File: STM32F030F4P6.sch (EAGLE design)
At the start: 11 parts, among them J3 455-1750-1-ND, U1 STM32F030F4P6, U2 CJA1117B-3.3-SOT89

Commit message: Added capacitors, resistors, diodes, LEDs, and J-Link connector.
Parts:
- added C2, C3, C4, C5, C6, C7: (no value), adafruit:C-USC0603
- added D2: (no value), adafruit:DIODESOD-123
- added J4: CORTEX_DEBUG_MINIMUM_PTH, SparkFun-Connectors:CORTEX_DEBUG_MINIMUM_PTH
- added LED2: (no value), adafruit:LEDCHIPLED_0603
- added R2, R3, R4, R5: (no value), adafruit:R-US_R0603
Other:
- moved on the sheet: C1
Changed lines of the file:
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@@
 <part name="SUPPLY1" library="SparkFun-PowerSymbols" deviceset="VDD" device=""/>
 <part name="GND1" library="SparkFun-PowerSymbols" deviceset="GND" device=""/>
+<part name="R2" library="adafruit" deviceset="R-US_" device="R0603"/>
+<part name="R3" library="adafruit" deviceset="R-US_" device="R0603"/>
+<part name="R4" library="adafruit" deviceset="R-US_" device="R0603"/>
+<part name="R5" library="adafruit" deviceset="R-US_" device="R0603"/>
+<part name="C2" library="adafruit" deviceset="C-US" device="C0603"/>
+<part name="C3" library="adafruit" deviceset="C-US" device="C0603"/>
+<part name="C4" library="adafruit" deviceset="C-US" device="C0603"/>
+<part name="C5" library="adafruit" deviceset="C-US" device="C0603"/>
+<part name="C6" library="adafruit" deviceset="C-US" device="C0603"/>
+<part name="C7" library="adafruit" deviceset="C-US" device="C0603"/>
+<part name="LED2" library="adafruit" deviceset="LED" device="CHIPLED_0603"/>
+<part name="D2" library="adafruit" deviceset="DIODE" device="SOD-123"/>
+<part name="J4" library="SparkFun-Connectors" deviceset="CORTEX_DEBUG_MINIMUM" device="_PTH"/>
 </parts>
 <sheets>
@@
 </plain>
 <instances>
-<instance part="C1" gate="G$1" x="71.12" y="15.24" smashed="yes">
-<attribute name="NAME" x="72.136" y="15.875" size="1.778" layer="95"/>
-<attribute name="VALUE" x="72.136" y="11.049" size="1.778" layer="96"/>
+<instance part="C1" gate="G$1" x="20.32" y="17.78" smashed="yes">
+<attribute name="NAME" x="21.336" y="18.415" size="1.778" layer="95"/>
+<attribute name="VALUE" x="21.336" y="13.589" size="1.778" layer="96"/>
 </instance>
 <instance part="R1" gate="G$1" x="99.06" y="15.24" smashed="yes">
@@
 <attribute name="VALUE" x="215.9" y="111.506" size="1.778" layer="96" align="top-center"/>
 </instance>
+<instance part="R2" gate="G$1" x="99.06" y="10.16" smashed="yes">
+<attribute name="NAME" x="95.25" y="11.6586" size="1.778" layer="95"/>
+<attribute name="VALUE" x="95.25" y="6.858" size="1.778" layer="96"/>
+</instance>
+<instance part="R3" gate="G$1" x="99.06" y="5.08" smashed="yes">
+<attribute name="NAME" x="95.25" y="6.5786" size="1.778" layer="95"/>
+<attribute name="VALUE" x="95.25" y="1.778" size="1.778" layer="96"/>
+</instance>
+<instance part="R4" gate="G$1" x="99.06" y="0" smashed="yes">
+<attribute name="NAME" x="95.25" y="1.4986" size="1.778" layer="95"/>
+<attribute name="VALUE" x="95.25" y="-3.302" size="1.778" layer="96"/>
+</instance>
+<instance part="R5" gate="G$1" x="99.06" y="-5.08" smashed="yes">
+<attribute name="NAME" x="95.25" y="-3.5814" size="1.778" layer="95"/>
+<attribute name="VALUE" x="95.25" y="-8.382" size="1.778" layer="96"/>
+</instance>
+<instance part="C2" gate="G$1" x="27.94" y="17.78" smashed="yes">
+<attribute name="NAME" x="28.956" y="18.415" size="1.778" layer="95"/>
+<attribute name="VALUE" x="28.956" y="13.589" size="1.778" layer="96"/>
+</instance>
+<instance part="C3" gate="G$1" x="35.56" y="17.78" smashed="yes">
+<attribute name="NAME" x="36.576" y="18.415" size="1.778" layer="95"/>
+<attribute name="VALUE" x="36.576" y="13.589" size="1.778" layer="96"/>
+</instance>
+<instance part="C4" gate="G$1" x="43.18" y="17.78" smashed="yes">
+<attribute name="NAME" x="44.196" y="18.415" size="1.778" layer="95"/>
+<attribute name="VALUE" x="44.196" y="13.589" size="1.778" layer="96"/>
+</instance>
+<instance part="C5" gate="G$1" x="50.8" y="17.78" smashed="yes">
+<attribute name="NAME" x="51.816" y="18.415" size="1.778" layer="95"/>
+<attribute name="VALUE" x="51.816" y="13.589" size="1.778" layer="96"/>
+</instance>
+<instance part="C6" gate="G$1" x="58.42" y="17.78" smashed="yes">
+<attribute name="NAME" x="59.436" y="18.415" size="1.778" layer="95"/>
+<attribute name="VALUE" x="59.436" y="13.589" size="1.778" layer="96"/>
+</instance>
+<instance part="C7" gate="G$1" x="66.04" y="17.78" smashed="yes">
+<attribute name="NAME" x="67.056" y="18.415" size="1.778" layer="95"/>
+<attribute name="VALUE" x="67.056" y="13.589" size="1.778" layer="96"/>
+</instance>
+<instance part="LED2" gate="G$1" x="129.54" y="17.78" smashed="yes" rot="MR0">
+<attribute name="NAME" x="125.984" y="13.208" size="1.778" layer="95" rot="MR90"/>
+<attribute name="VALUE" x="123.825" y="13.208" size="1.778" layer="96" rot="MR90"/>
+</instance>
+<instance part="D2" gate="G$1" x="185.42" y="106.68" smashed="yes">
+<attribute name="NAME" x="182.88" y="109.22" size="1.27" layer="95"/>
+<attribute name="VALUE" x="182.88" y="102.87" size="1.27" layer="96"/>
+</instance>
+<instance part="J4" gate="G$1" x="223.52" y="88.9" smashed="yes">
+<attribute name="NAME" x="213.36" y="96.774" size="1.778" layer="95" font="vector"/>
+<attribute name="VALUE" x="213.36" y="81.534" size="1.778" layer="96" font="vector"/>
+</instance>
 </instances>

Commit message: Connected all components.
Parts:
- added C8: (no value), adafruit:C-USC0603
- added FRAME1: FRAME-LETTER, SparkFun-Aesthetics:FRAME-LETTER
- added J5: (no value), SparkFun-Connectors:CONN_02
- J1: device SparkFun-Connectors:CONN_10" -> SparkFun-Connectors:CONN_11
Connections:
- new net N$1: J3.2, R1.1
- new net N$3: C6.1, R2.1, Y1.1
- new net N$5: D2.A, U2.OUT
- new net N$7: LED1.C, R3.2
- new net N$8: LED2.C, R4.1
- new net VIN_2.4-3.6V: D1.A, J2.7
- new net VIN_5-30V: C1.1, J1.1, U2.IN
- net A0: now also J1.7, J5.1, J5.2, LED2.A; no longer J1.6
- net A1: now also J1.8; no longer J1.7
- net A10: now also J2.6; no longer J2.3
- net A2: now also J1.9; no longer J1.8
- net A3: now also J1.10; no longer J1.9
- net A4: now also J1.11; no longer J1.10
- net A5: now also J2.1; no longer J2.10
- net A6: now also J2.2; no longer J2.9
- net A7: now also J2.3; no longer J2.8
- net A9: now also J2.5; no longer J2.4
- net B1: now also J2.4; no longer J2.7
- net BOOT0: now also J1.2, R1.2; no longer J1.1
- net GND: now also C1.2, C2.2, C3.2, C4.2, C5.2, C6.2, C7.2, C8.2, J2.8, J3.1, J4.GND, R3.1, R4.2, S1.1, U2.GND; no longer J2.6
- net NRST: now also C7.1, J1.5, J4.!RESET, S1.2; no longer J1.4
- net OSC_IN: now also C5.1, J1.3, Y1.2; no longer J1.2
- net OSC_OUT: now also J1.4, R2.2; no longer J1.3
- net SWCLK: now also J2.10, J4.SWDCLK; no longer J2.1
- net SWDIO: now also J2.9, J4.SWDIO; no longer J2.2
- net VDD: now also C2.1, C3.1, D1.C, D2.C, J3.3, J4.VCC, LED1.A, R5.1; no longer J2.5
- net VDDA: now also C4.1, C8.1, J1.6, R5.2; no longer J1.5
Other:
- note added: "Nathan Jones, nathancharlesjones@gmail.com"
- moved on the sheet: C1, C2, C3, C4, C5, C6, C7, D1, D2, J2, J3, J4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

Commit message: Initial placement. Added diode between VDD and VDDA. Added pulldown resistor to BOOT0.
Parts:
- removed R5: (no value), adafruit:R-US_R0603
- removed U2: CJA1117B-3.3-SOT89, OPL_IC:PMIC-CJA1117B-3.3(SOT-89)
- added D3: (no value), diode:DIODE-DO-214AC
- added IC1: MCP170333MB, linear:MCP170333MB
- added R6: (no value), adafruit:R-US_R0603
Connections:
- net A0: now also J1.6; no longer J1.7
- net A1: now also J1.7; no longer J1.8
- net A10: now also J2.5; no longer J2.6
- net A2: now also J1.8; no longer J1.9
- net A3: now also J1.9; no longer J1.10
- net A4: now also J1.10; no longer J1.11
- net A5: now also J1.11; no longer J2.1
- net A6: now also J2.1; no longer J2.2
- net A7: now also J2.2; no longer J2.3
- net A9: now also J2.4; no longer J2.5
- net B1: now also J2.3; no longer J2.4
- net GND: now also IC1.GND, J2.9, R6.1; no longer J2.8, U2.GND
- net N$1: now also R6.2
- net N$5: now also IC1.VO; no longer U2.OUT
- net NRST: now also J2.6; no longer J1.5
- net SWCLK: now also J2.8; no longer J2.10
- net SWDIO: now also J2.7; no longer J2.9
- net VDD: now also D3.A; no longer R5.1
- net VDDA: now also D3.C, J1.5; no longer J1.6, R5.2
- net VIN_2.4-3.6V: now also J2.10; no longer J2.7
- net VIN_5-30V: now also IC1.VI1; no longer U2.IN
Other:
- moved on the sheet: R1

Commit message: Finished.
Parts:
- removed FRAME1: FRAME-LETTER, SparkFun-Aesthetics:FRAME-LETTER
- removed J5: (no value), SparkFun-Connectors:CONN_02
- added FRAME2: FRAME-LETTERNO_PACKAGE, SparkFun-Aesthetics:FRAME-LETTERNO_PACKAGE
- C1: value (none) -> 10uF
- C2: value (none) -> 4.7uF
- C3, C8: value (none) -> 100nF
- C4: value (none) -> 1uF
- C5: value (none) -> 10nF
- C6, C7: value (none) -> 20pF
- J1: device SparkFun-Connectors:CONN_11 -> SparkFun-Connectors:CONN_19
- J2: value (none) -> 455-1750-1-ND; device SparkFun-Connectors:CONN_10" -> SparkFun-Connectors:CONN_03
- J3: value 455-1750-1-ND -> (none); device SparkFun-Connectors:CONN_03 -> SparkFun-Connectors:CONN_02
- R1, R2: value (none) -> 100R
- R3: value (none) -> 1k
- R4: value (none) -> 10k
- R5: value (none) -> 0R
- renumbered R6 to R5
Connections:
- removed net N$8: LED2.C, R4.1
- new net N$2: J3.1, J3.2, LED2.C, R2.1
- net A0: now also J1.3; no longer J1.6, J5.1, J5.2
- net A1: now also J1.4; no longer J1.7
- net A10: now also J1.13; no longer J2.5
- net A2: now also J1.5; no longer J1.8
- net A3: now also J1.6; no longer J1.9
- net A4: now also J1.7; no longer J1.10
- net A5: now also J1.8; no longer J1.11
- net A6: now also J1.9; no longer J2.1
- net A7: now also J1.10; no longer J2.2
- net A9: now also J1.12; no longer J2.4
- net B1: now also J1.11; no longer J2.3
- net BOOT0: now also J1.1, R4.2; no longer J1.2, R1.2
- net GND: now also J1.17, J2.1, R1.1, R2.2; no longer J2.9, J3.1, R3.1, R4.2
- net N$1: now also J2.2, R4.1; no longer J3.2, R1.1
- net N$3: now also R3.1; no longer R2.1
- net N$7: now also R1.2; no longer R3.2
- net NRST: now also C8.1, J1.14; no longer C7.1, J2.6
- net OSC_IN: now also C7.1; no longer C5.1, J1.3
- net OSC_OUT: now also R3.2; no longer J1.4, R2.2
- net SWCLK: now also J1.16; no longer J2.8
- net SWDIO: now also J1.15; no longer J2.7
- net VDD: now also J2.3; no longer J3.3
- net VDDA: now also C5.1, J1.2; no longer C8.1, J1.5
- net VIN_2.4-3.6V: now also J1.18; no longer J2.10
- net VIN_5-30V: now also J1.19; no longer J1.1
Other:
- note removed: "Nathan Jones, nathancharlesjones@gmail.com"
- moved on the sheet: C5, C7, C8, LED2, R1, R2, R3, R4, S1

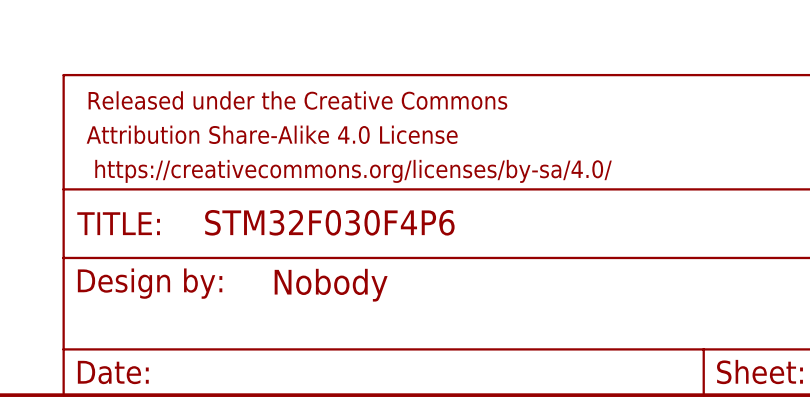
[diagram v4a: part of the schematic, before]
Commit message: Added schematic PDF and PNG and README.
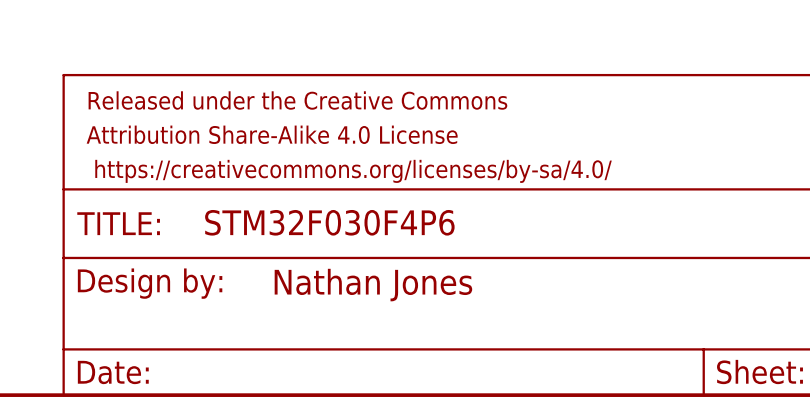
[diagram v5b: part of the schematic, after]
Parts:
- FRAME2: DESIGNER (none) -> Nathan Jones
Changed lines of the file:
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@@
 <part name="D3" library="diode" library_urn="urn:adsk.eagle:library:210" deviceset="DIODE-" device="DO-214AC" package3d_urn="urn:adsk.eagle:package:43416/2"/>
 <part name="IC1" library="linear" library_urn="urn:adsk.eagle:library:262" deviceset="MCP1703*" device="MB" package3d_urn="urn:adsk.eagle:package:16478/2" technology="33"/>
-<part name="FRAME2" library="SparkFun-Aesthetics" deviceset="FRAME-LETTER" device="NO_PACKAGE"/>
+<part name="FRAME2" library="SparkFun-Aesthetics" deviceset="FRAME-LETTER" device="NO_PACKAGE">
+<attribute name="DESIGNER" value="Nathan Jones"/>
+</part>
 <part name="J1" library="SparkFun-Connectors" deviceset="CONN_19" device=""/>
 </parts>
